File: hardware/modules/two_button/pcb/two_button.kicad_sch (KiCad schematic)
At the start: 7 parts, among them SW1 SW_Push, SW2 SW_Push

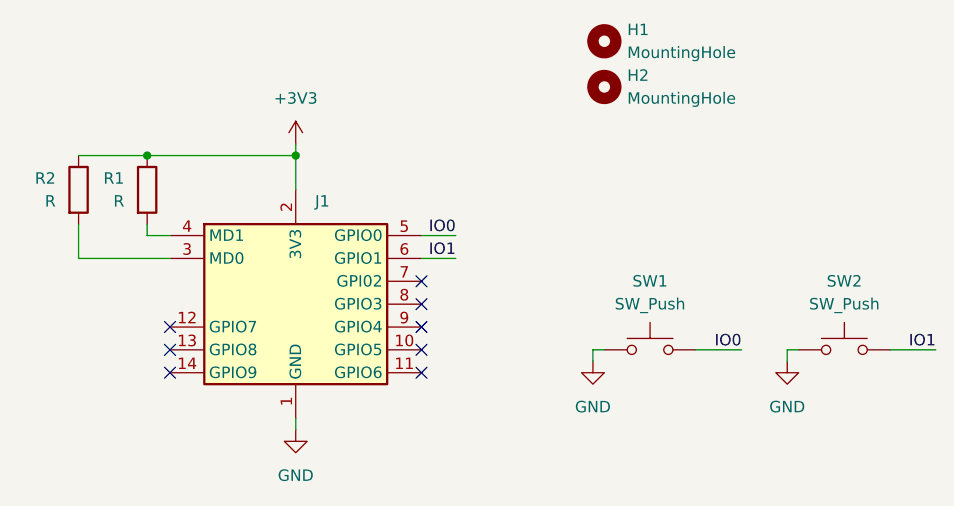
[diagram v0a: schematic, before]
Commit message: added resistor values to the four and two button modules
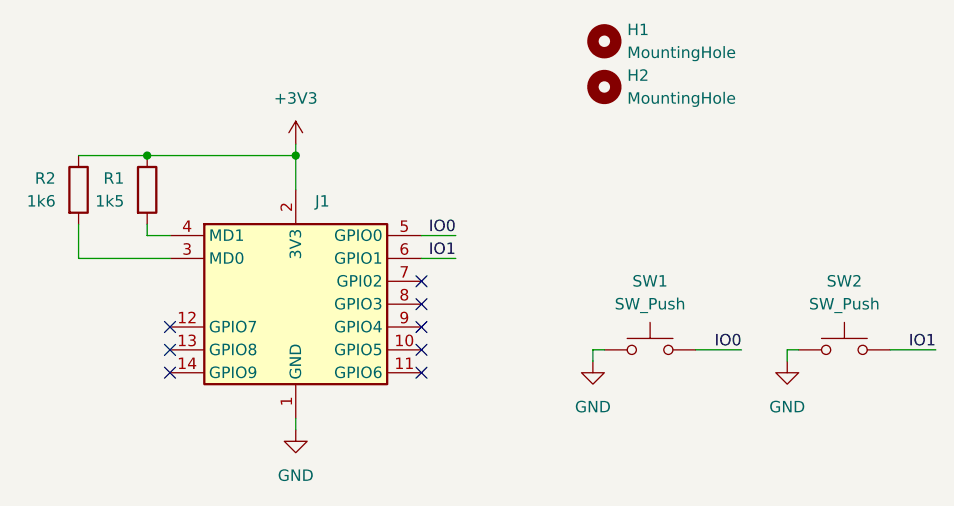
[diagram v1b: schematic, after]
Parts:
- R1: value R -> 1k5; LCSC (none) -> C281775
- R2: value R -> 1k6; LCSC (none) -> C861205
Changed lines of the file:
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@@
+	(wire
+		(pts
+			(xy 69.85 76.2) (xy 86.36 76.2)
+		)
+		(stroke
+			(width 0)
+			(type default)
+		)
+	)
 	(wire
 		(pts
@@
 		(pts
 			(xy 86.36 74.93) (xy 86.36 76.2)
-		)
-		(stroke
-			(width 0)
-			(type default)
-		)
-	)
-	(wire
-		(pts
-			(xy 69.85 76.2) (xy 86.36 76.2)
 		)
 		(stroke
@@
 	)
 	(symbol
+		(lib_id "Device:R")
+		(at 69.85 80.01 0)
+		(unit 1)
+		(body_style 1)
+		(exclude_from_sim no)
+		(in_bom yes)
+		(on_board yes)
+		(in_pos_files yes)
+		(dnp no)
+		(property "Reference" "R1"
+			(at 67.31 78.7399 0)
+			(show_name no)
+			(do_not_autoplace no)
+			(effects
+				(font
+					(size 1.27 1.27)
+				)
+				(justify right)
+			)
+		)
+		(property "Value" "1k5"
+			(at 67.31 81.2799 0)
+			(show_name no)
+			(do_not_autoplace no)
+			(effects
+				(font
+					(size 1.27 1.27)
+				)
+				(justify right)
+			)
+		)
+		(property "Footprint" "Resistor_SMD:R_0805_2012Metric_Pad1.20x1.40mm_HandSolder"
+			(at 68.072 80.01 90)
+			(hide yes)
+			(show_name no)
+			(do_not_autoplace no)
+			(effects
+				(font
+					(size 1.27 1.27)
+				)
+			)
+		)
+		(property "Datasheet" ""
+			(at 69.85 80.01 0)
+			(hide yes)
+			(show_name no)
+			(do_not_autoplace no)
+			(effects
+				(font
+					(size 1.27 1.27)
+				)
+			)
+		)
+		(property "Description" "Resistor"
+			(at 69.85 80.01 0)
+			(hide yes)
+			(show_name no)
+			(do_not_autoplace no)
+			(effects
+				(font
+					(size 1.27 1.27)
+				)
+			)
+		)
+		(property "LCSC" "C281775"
+			(at 69.85 80.01 0)
+			(hide yes)
+			(show_name no)
+			(do_not_autoplace no)
+			(effects
+				(font
+					(size 1.27 1.27)
+				)
+			)
+		)
+		(pin "1"
+		)
+		(pin "2"
+		)
+		(instances
+			(project "two_button"
+				(path "/4f0f379b-9acc-49b4-81dc-86c4ce2d2a86"
+					(reference "R1")
+					(unit 1)
+				)
+			)
+		)
+	)
+	(symbol
+		(lib_id "Device:R")
+		(at 62.23 80.01 0)
+		(unit 1)
+		(body_style 1)
+		(exclude_from_sim no)
+		(in_bom yes)
+		(on_board yes)
+		(in_pos_files yes)
+		(dnp no)
+		(property "Reference" "R2"
+			(at 59.69 78.7399 0)
+			(show_name no)
+			(do_not_autoplace no)
+			(effects
+				(font
+					(size 1.27 1.27)
+				)
+				(justify right)
+			)
+		)
+		(property "Value" "1k6"
+			(at 59.69 81.2799 0)
+			(show_name no)
+			(do_not_autoplace no)
+			(effects
+				(font
+					(size 1.27 1.27)
+				)
+				(justify right)
+			)
+		)
+		(property "Footprint" "Resistor_SMD:R_0805_2012Metric_Pad1.20x1.40mm_HandSolder"
+			(at 60.452 80.01 90)
+			(hide yes)
+			(show_name no)
+			(do_not_autoplace no)
+			(effects
+				(font
+					(size 1.27 1.27)
+				)
+			)
+		)
+		(property "Datasheet" ""
+			(at 62.23 80.01 0)
+			(hide yes)
+			(show_name no)
+			(do_not_autoplace no)
+			(effects
+				(font
+					(size 1.27 1.27)
+				)
+			)
+		)
+		(property "Description" "Resistor"
+			(at 62.23 80.01 0)
+			(hide yes)
+			(show_name no)
+			(do_not_autoplace no)
+			(effects
+				(font
+					(size 1.27 1.27)
+				)
+			)
+		)
+		(property "LCSC" "C861205"
+			(at 62.23 80.01 0)
+			(hide yes)
+			(show_name no)
+			(do_not_autoplace no)
+			(effects
+				(font
+					(size 1.27 1.27)
+				)
+			)
+		)
+		(pin "1"
+		)
+		(pin "2"
+		)
+		(instances
+			(project "two_button"
+				(path "/4f0f379b-9acc-49b4-81dc-86c4ce2d2a86"
+					(reference "R2")
+					(unit 1)
+				)
+			)
+		)
+	)
+	(symbol
 		(lib_id "power:+3V3")
 		(at 86.36 74.93 0)
@@
 				(path "/4f0f379b-9acc-49b4-81dc-86c4ce2d2a86"
 					(reference "#PWR04")
-					(unit 1)
-				)
-			)
-		)
-	)
-	(symbol
-		(lib_id "Device:R")
-		(at 69.85 80.01 0)
-		(unit 1)
-		(body_style 1)
-		(exclude_from_sim no)
-		(in_bom yes)
-		(on_board yes)
-		(in_pos_files yes)
-		(dnp no)
-		(property "Reference" "R1"
-			(at 67.31 78.7399 0)
-			(show_name no)
-			(do_not_autoplace no)
-			(effects
-				(font
-					(size 1.27 1.27)
-				)
-				(justify right)
-			)
-		)
-		(property "Value" "R"
-			(at 67.31 81.2799 0)
-			(show_name no)
-			(do_not_autoplace no)
-			(effects
-				(font
-					(size 1.27 1.27)
-				)
-				(justify right)
-			)
-		)
-		(property "Footprint" "Resistor_SMD:R_0805_2012Metric_Pad1.20x1.40mm_HandSolder"
-			(at 68.072 80.01 90)
-			(hide yes)
-			(show_name no)
-			(do_not_autoplace no)
-			(effects
-				(font
-					(size 1.27 1.27)
-				)
-			)
-		)
-		(property "Datasheet" ""
-			(at 69.85 80.01 0)
-			(hide yes)
-			(show_name no)
-			(do_not_autoplace no)
-			(effects
-				(font
-					(size 1.27 1.27)
-				)
-			)
-		)
-		(property "Description" "Resistor"
-			(at 69.85 80.01 0)
-			(hide yes)
-			(show_name no)
-			(do_not_autoplace no)
-			(effects
-				(font
-					(size 1.27 1.27)
-				)
-			)
-		)
-		(pin "1"
-		)
-		(pin "2"
-		)
-		(instances
-			(project "two_button"
-				(path "/4f0f379b-9acc-49b4-81dc-86c4ce2d2a86"
-					(reference "R1")
 					(unit 1)
 				)
@@
 					(unit 1)
 				)
-			)
-		)
-	)
-	(symbol
-		(lib_id "Device:R")
-		(at 62.23 80.01 0)
-		(unit 1)
-		(body_style 1)
-		(exclude_from_sim no)
-		(in_bom yes)
-		(on_board yes)
-		(in_pos_files yes)
-		(dnp no)
-		(property "Reference" "R2"
-			(at 59.69 78.7399 0)
-			(show_name no)
-			(do_not_autoplace no)
-			(effects
-				(font
-					(size 1.27 1.27)
-				)
-				(justify right)
-			)
-		)
-		(property "Value" "R"
-			(at 59.69 81.2799 0)
-			(show_name no)
-			(do_not_autoplace no)
-			(effects
-				(font
-					(size 1.27 1.27)
-				)
-				(justify right)
-			)
-		)
-		(property "Footprint" "Resistor_SMD:R_0805_2012Metric_Pad1.20x1.40mm_HandSolder"
-			(at 60.452 80.01 90)
-			(hide yes)
-			(show_name no)
-			(do_not_autoplace no)
-			(effects
-				(font
-					(size 1.27 1.27)
-				)
-			)
-		)
-		(property "Datasheet" ""
-			(at 62.23 80.01 0)
-			(hide yes)
-			(show_name no)
-			(do_not_autoplace no)
-			(effects
-				(font
-					(size 1.27 1.27)
-				)
-			)
-		)
-		(property "Description" "Resistor"
-			(at 62.23 80.01 0)
-			(hide yes)
-			(show_name no)
-			(do_not_autoplace no)
-			(effects
-				(font
-					(size 1.27 1.27)
-				)
-			)
-		)
-		(pin "1"
-		)
-		(pin "2"
-		)
-		(instances
-			(project "two_button"
-				(path "/4f0f379b-9acc-49b4-81dc-86c4ce2d2a86"
-					(reference "R2")
-					(unit 1)
-				)

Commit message: updated lcsc part nums for modules with correct footprint
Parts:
- R1: LCSC C281775 -> C126687
- R2: LCSC C861205 -> C473287
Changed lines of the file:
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@@
 			)
 		)
-		(property "LCSC" "C281775"
+		(property "LCSC" "C126687"
 			(at 69.85 80.01 0)
 			(hide yes)
@@
 			)
 		)
-		(property "LCSC" "C861205"
+		(property "LCSC" "C473287"
 			(at 62.23 80.01 0)
 			(hide yes)
